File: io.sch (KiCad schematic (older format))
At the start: 16 parts, among them P1 CONN_01X08, P2 CONN_02X08, X1 CON-JST_SM04B-SRSS-TB, X2 CON-JST_SM04B-SRSS-TB, X4 CON-JST_SM04B-SRSS-TB

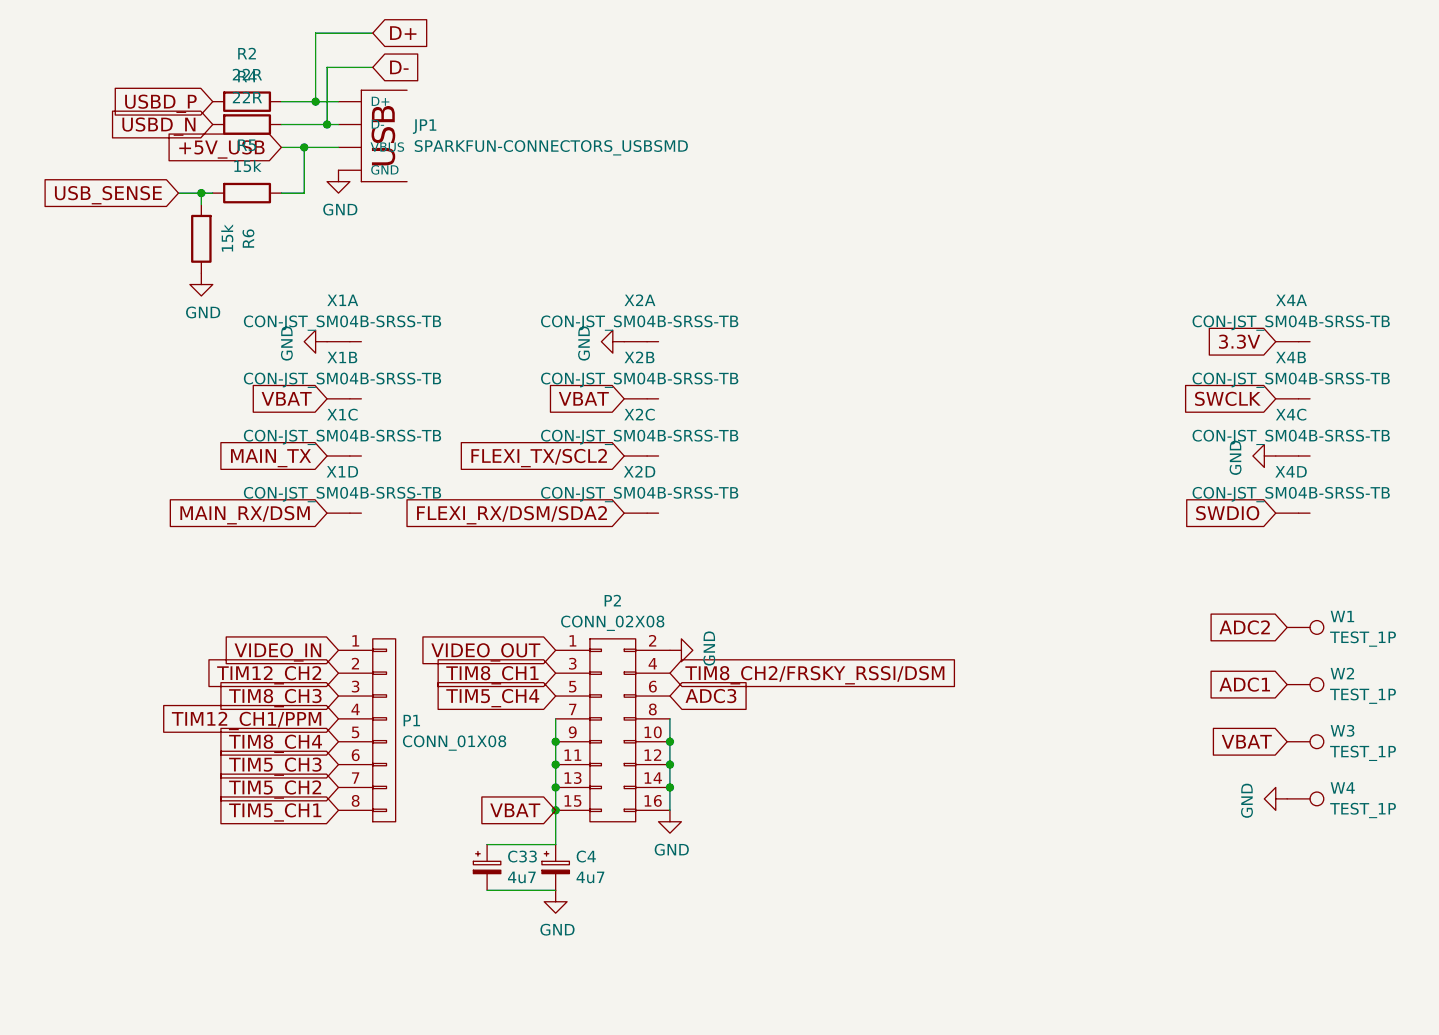
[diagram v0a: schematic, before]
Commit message: routing finished - essential signals only
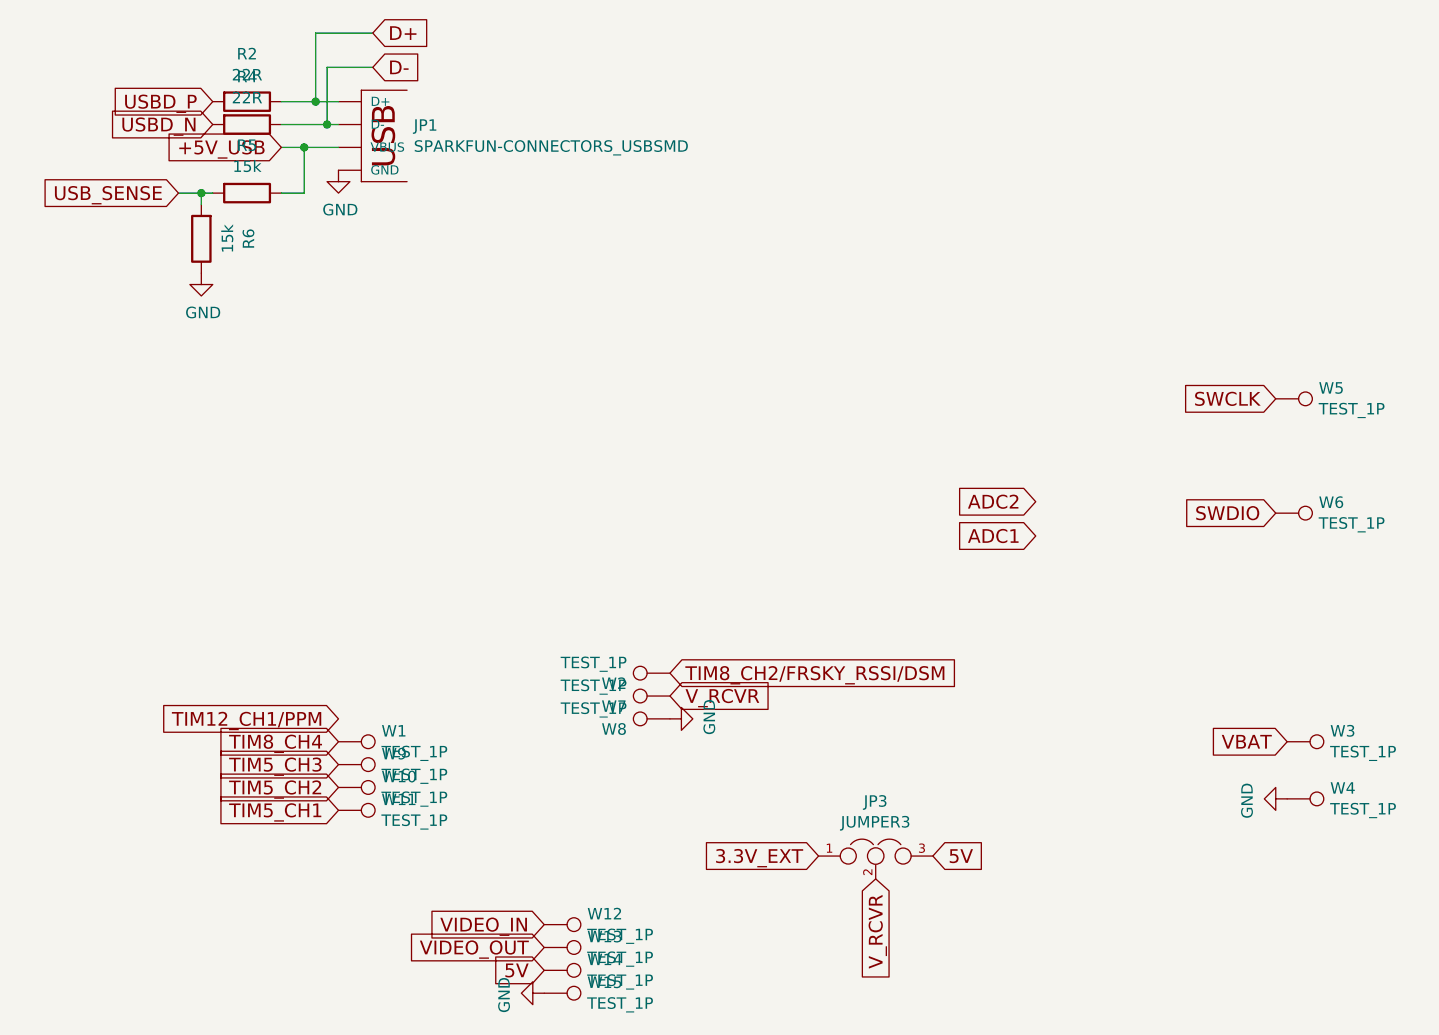
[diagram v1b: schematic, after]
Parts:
- removed C33, C4: 4u7, Capacitors_Tantalum_SMD:TantalC_SizeA_EIA-3216_Reflow, symbol CP_Small
- removed P1: CONN_01X08, Pin_Headers:Pin_Header_Straight_1x08, symbol CONN_01X08
- removed P2: CONN_02X08, Pin_Headers:Pin_Header_Straight_2x08, symbol CONN_02X08
- removed X1, X2, X4: CON-JST_SM04B-SRSS-TB, Connectors_JST_SH:Connectors_JST_SM04B-SRSS-TB, symbol CON-JST_SM04B-SRSS-TB
- added JP3: JUMPER3, minimal:SPARKFUN-PASSIVES_PAD-JUMPER-3-2OF3_NC_BY_PASTE_YES_SILK_FULL_BOX, symbol JUMPER3
- added W10, W11, W12, W13, W14, W15, W7, W8, W9: TEST_1P, alis_parts:pad_2x1.5mm, symbol TEST_1P
- added W5, W6: TEST_1P, alis_parts:pad_round_1mm, symbol TEST_1P
- JP1: footprint minimal:SPARKFUN-CONNECTORS_USB-MINIB -> alis_parts:micro_usb
- R2, R4, R5, R6: footprint Resistors_SMD:R_0603 -> Resistors_SMD:R_0402
- W1, W2: footprint Measurement_Points:Measurement_Point_Square-SMD-Pad_Big -> alis_parts:pad_2x1.5mm
- W3, W4: footprint Measurement_Points:Measurement_Point_Square-SMD-Pad_Big -> alis_parts:battery_pad
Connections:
- net ADC1: no longer W2.1
- net ADC2: no longer W1.1
- net GND: now also W15.1, W8.1
- net SWCLK: now also W5.1
- net SWDIO: now also W6.1
- net TIM5_CH1: now also W11.1
- net TIM5_CH2: now also W10.1
- net TIM5_CH3: now also W9.1
- net TIM8_CH2/FRSKY_RSSI/DSM: now also W2.1
- net TIM8_CH4: now also W1.1
- net VIDEO_IN: now also W12.1
- net VIDEO_OUT: now also W13.1
- new net 3.3V_EXT: JP3.1
- new net 5V: JP3.3, W14.1
- new net V_RCVR: JP3.2, W7.1
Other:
- moved on the sheet: W1, W2

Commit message: minor changes
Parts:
- added R29, R30: 10k, Resistors_SMD:R_0402, symbol R
- R5, R6: value 15k -> 10k
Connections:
- net ADC1: now also R29.2, R30.2
- net GND: now also R30.1
- net VBAT: now also R29.1
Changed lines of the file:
@@
 P 3150 2200
 F 0 "R5" V 2942 2200 50  0000 C CNN
-F 1 "15k" V 3034 2200 50  0000 C CNN
+F 1 "10k" V 3034 2200 50  0000 C CNN
 F 2 "Resistors_SMD:R_0402" V 3080 2200 50  0001 C CNN
 F 3 "" H 3150 2200 50  0000 C CNN
@@
 P 2950 2400
 F 0 "R6" V 2742 2400 50  0000 C CNN
-F 1 "15k" V 2834 2400 50  0000 C CNN
+F 1 "10k" V 2834 2400 50  0000 C CNN
 F 2 "Resistors_SMD:R_0402" V 2880 2400 50  0001 C CNN
 F 3 "" H 2950 2400 50  0000 C CNN
@@
 	2950 2250 2950 2200
 Connection ~ 2950 2200
-Text GLabel 6600 3700 0    60   Input ~ 0
+Text GLabel 3900 3300 0    60   Input ~ 0
 ADC1
 Text GLabel 6600 3550 0    60   Input ~ 0
@@
 	0    1    1    0
 $EndComp
+$Comp
+L R R30
+U 1 1 57616BA1
+P 3900 3450
+F 0 "R30" V 3692 3450 50  0000 C CNN
+F 1 "10k" V 3784 3450 50  0000 C CNN
+F 2 "Resistors_SMD:R_0402" V 3830 3450 50  0001 C CNN
+F 3 "" H 3900 3450 50  0000 C CNN
+	1    3900 3450
+	-1   0    0    1
+$EndComp
+$Comp
+L R R29
+U 1 1 57616C57
+P 4050 3300
+F 0 "R29" V 3842 3300 50  0000 C CNN
+F 1 "10k" V 3934 3300 50  0000 C CNN
+F 2 "Resistors_SMD:R_0402" V 3980 3300 50  0001 C CNN
+F 3 "" H 4050 3300 50  0000 C CNN
+	1    4050 3300
+	0    1    1    0
+$EndComp
+$Comp
+L GND #PWR06
+U 1 1 57616D0A
+P 3900 3600
+F 0 "#PWR06" H 3900 3350 50  0001 C CNN
+F 1 "GND" H 3908 3426 50  0000 C CNN
+F 2 "" H 3900 3600 50  0000 C CNN
+F 3 "" H 3900 3600 50  0000 C CNN
+	1    3900 3600
+	1    0    0    -1
+$EndComp
+Text GLabel 4200 3300 2    60   Input ~ 0
+VBAT
 $EndSCHEMATC
